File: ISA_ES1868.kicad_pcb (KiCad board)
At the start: 4 copper layers, 104.1 x 99.1 mm, 105 parts, among them J1 LINE IN, J10 Vol. Btns, J11 ISA BUS, J2 MIC, J3 Joystick/MIDI, J5 Wavetable, J7 SPKR OUT, J8 LINE OUT, U1 L78L05, U2 74LS138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

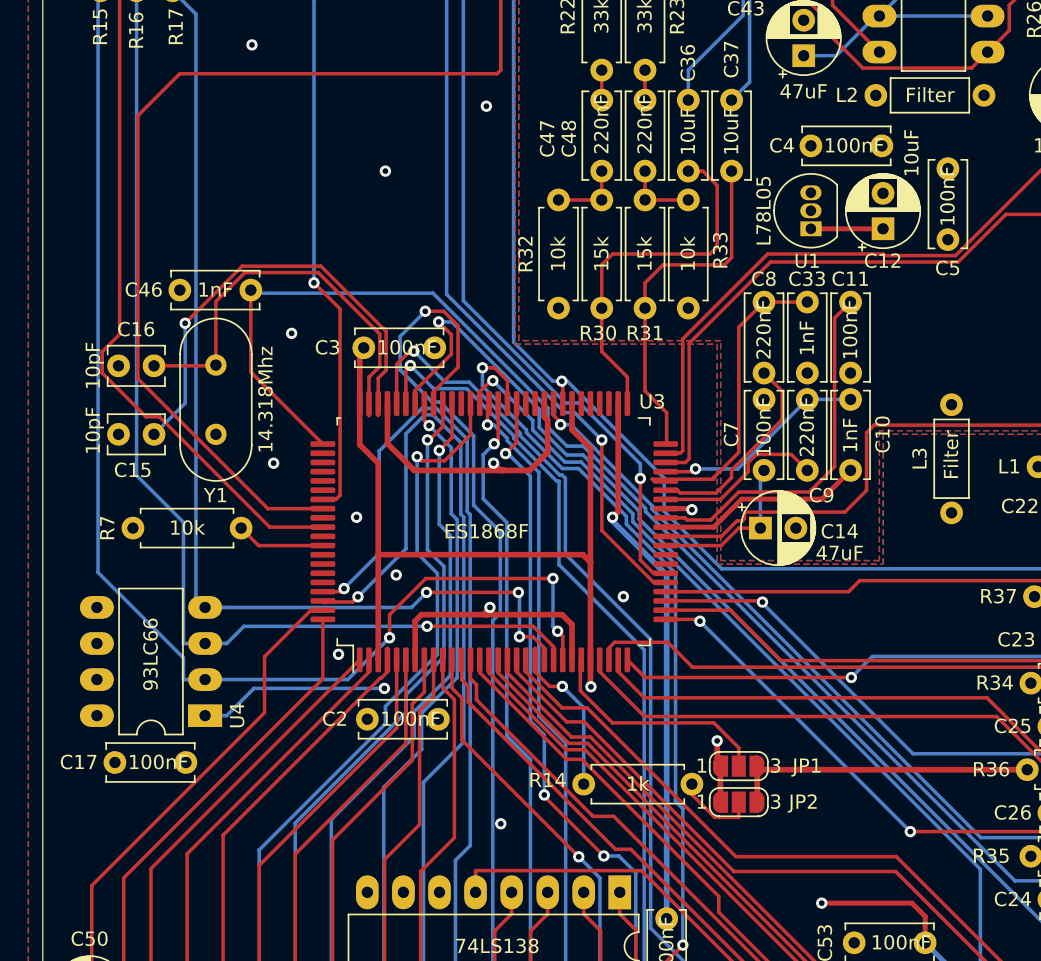
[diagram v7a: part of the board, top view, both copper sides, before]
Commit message: More silkscreen adjustments
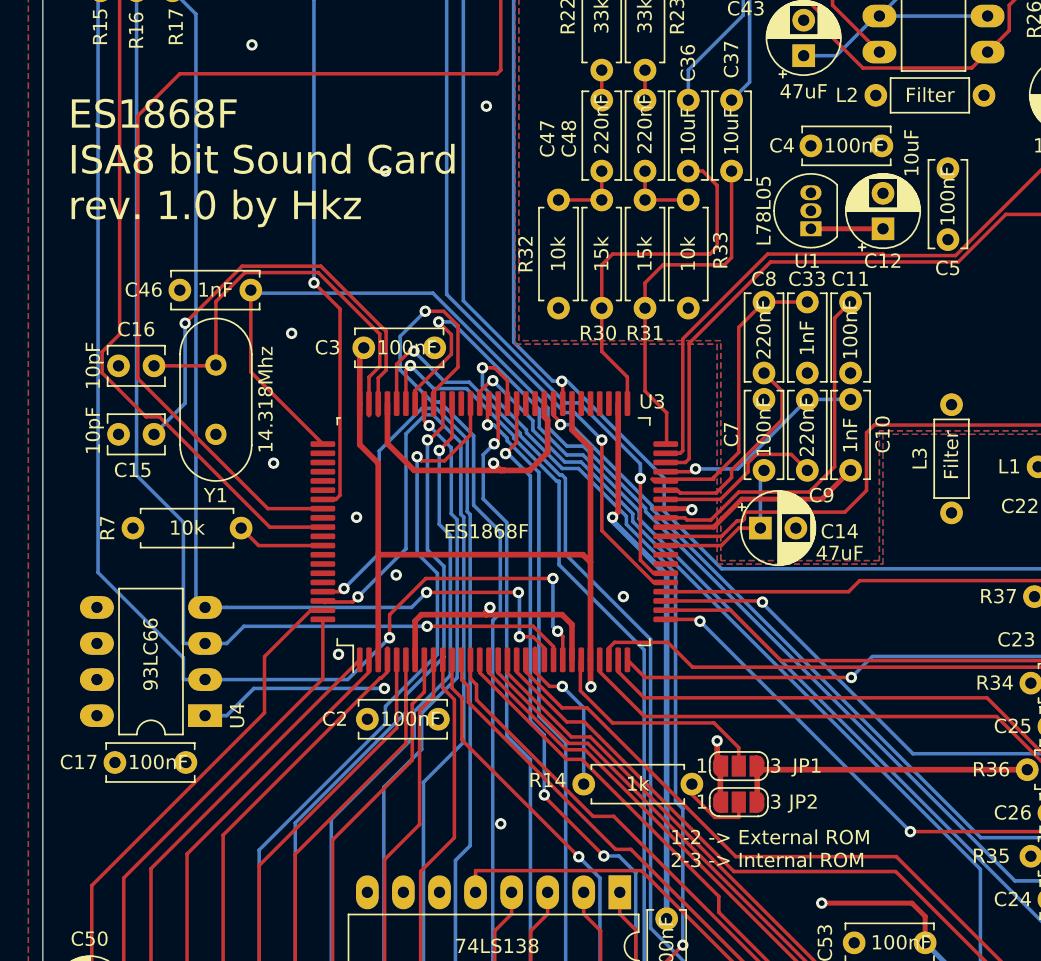
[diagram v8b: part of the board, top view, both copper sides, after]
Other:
- board text added: "1-2 -> External ROM 2-3 -> Internal ROM"
- board text added: "ES1868F ISA8 bit Sound Card rev. 1.0 by Hkz"
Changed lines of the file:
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@@
   (general
     (thickness 1.6)
-    (drawings 14)
+    (drawings 16)
     (tracks 1355)
     (zones 0)
@@
     )
   )
+  (gr_text "ES1868F\nISA8 bit Sound Card\nrev. 1.0 by Hkz" (at 212.598 131.572) (layer F.SilkS)
+    (effects (font (size 2 2) (thickness 0.3)) (justify left))
+  )
+  (gr_text "1-2 -> External ROM\n2-3 -> Internal ROM" (at 255.016 180.086) (layer F.SilkS)
+    (effects (font (size 1 1) (thickness 0.15)) (justify left))
+  )
   (dimension 8.636 (width 0.15) (layer Dwgs.User)
